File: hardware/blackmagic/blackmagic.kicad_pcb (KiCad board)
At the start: 2 copper layers, 28 parts, among them U1 STM32F411CEUx, U2 USBLC6-2P6, U3 AP2112K-3.3TRG1

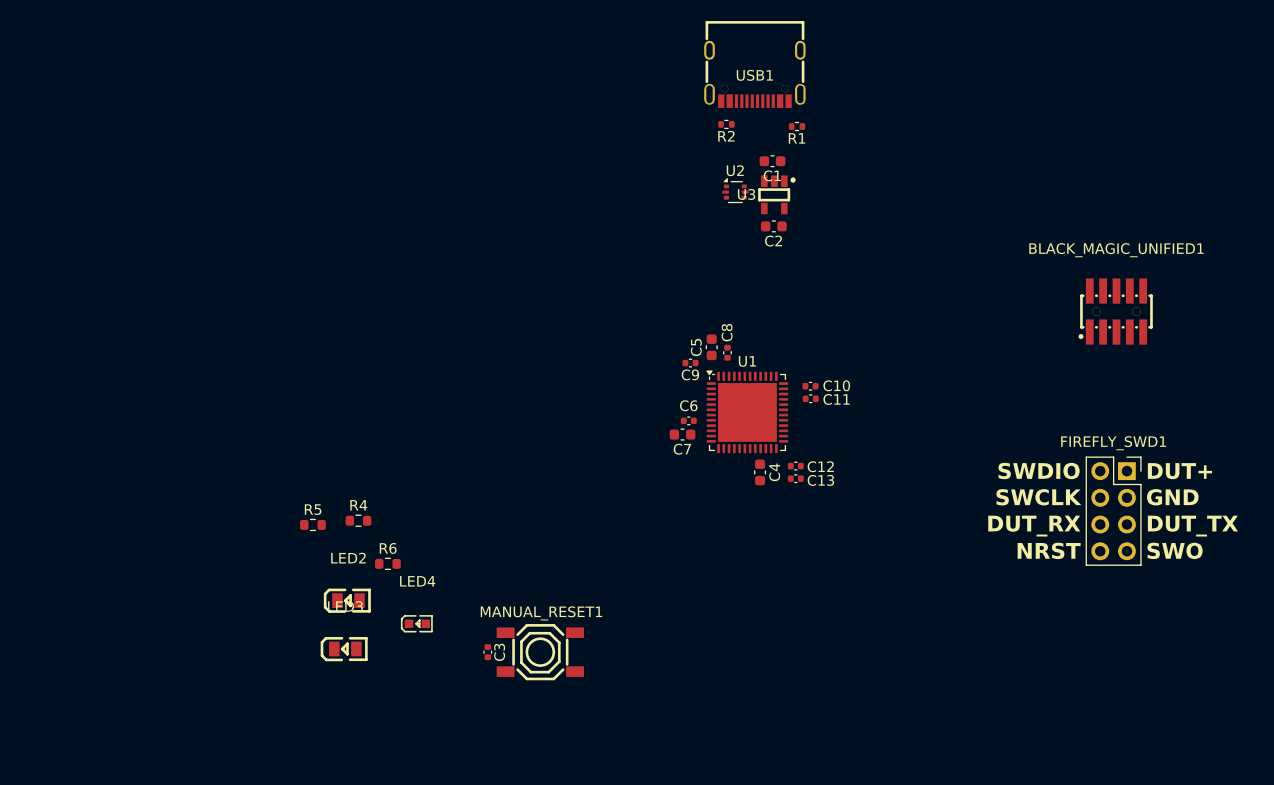
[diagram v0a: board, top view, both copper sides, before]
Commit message: Finish with the first pass of the routing
Still need to add some GND vias and clean things up
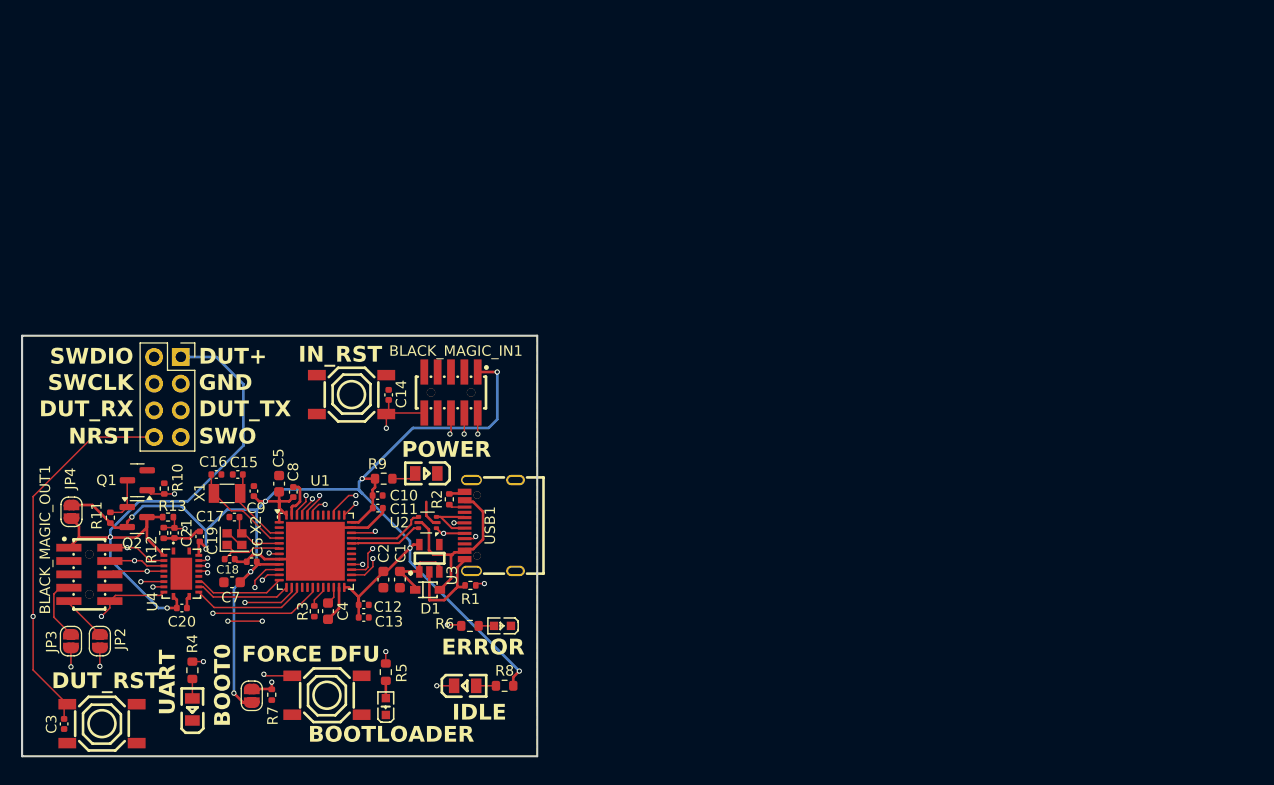
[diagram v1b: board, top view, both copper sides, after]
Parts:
- removed BLACK_MAGIC_UNIFIED1: KH-1.27PH180-2X5P-L7.2-SMT, easyeda2kicad:HDR-SMD_10P-P1.27-V-M-R2-C5-LS5.5
- removed FIREFLY_SWD1: Conn_01x08_Female, Connector_PinSocket_2.54mm:PinSocket_2x04_P2.54mm_Vertical
- removed MANUAL_RESET1: TS-1187A-B-A-B, easyeda2kicad:SW-SMD_4P-L5.1-W5.1-P3.70-LS6.5-TL-2
- added BLACK_MAGIC_IN1: KH-1.27PH180-2X5P-L7.2-SMT, easyeda2kicad:HDR-SMD_10P-P1.27-V-M-R2-C5-LS5.5, F.Cu at (140.8, 105.4)
- added BLACK_MAGIC_OUT1: KH-1.27PH180-2X5P-L7.2-SMT, easyeda2kicad:HDR-SMD_10P-P1.27-V-M-R2-C5-LS5.5, F.Cu at (106.4, 122.7)
- added C14: 100 nF, Capacitor_SMD:C_0402_1005Metric, F.Cu at (134.9, 105.6)
- added C15: 12 pF, Capacitor_SMD:C_0402_1005Metric, F.Cu at (120.5, 113.2)
- added C16: 12 pF, Capacitor_SMD:C_0402_1005Metric, F.Cu at (118.5, 113.2)
- added C17: 12 pF, Capacitor_SMD:C_0402_1005Metric, F.Cu at (120.2, 117.2)
- added C18: 12 pF, Capacitor_SMD:C_0402_1005Metric, F.Cu at (119.8, 121.2)
- added C19: 100 nF, Capacitor_SMD:C_0402_1005Metric, F.Cu at (116.9, 119.1)
- added C20: 100 nF, Capacitor_SMD:C_0402_1005Metric, F.Cu at (115.2, 125.9)
- added C21: 100 nF, Capacitor_SMD:C_0402_1005Metric, F.Cu at (114.5, 118.8)
- added D1: Schottky 1A 40V, easyeda2kicad:SOD-323_L1.8-W1.3-LS2.5-RD, F.Cu at (138.6, 124.2)
- added JP1: SolderJumper_2_Open, Jumper:SolderJumper-2_P1.3mm_Open_RoundedPad1.0x1.5mm, F.Cu at (121.8, 134.2)
- added JP2: SolderJumper_2_Open, Jumper:SolderJumper-2_P1.3mm_Open_RoundedPad1.0x1.5mm, F.Cu at (104.7, 129.1)
- added JP3: SolderJumper_2_Open, Jumper:SolderJumper-2_P1.3mm_Open_RoundedPad1.0x1.5mm, F.Cu at (107.4, 129.1)
- added JP4: SolderJumper_2_Open, Jumper:SolderJumper-2_P1.3mm_Open_RoundedPad1.0x1.5mm, F.Cu at (104.7, 116.8)
- added LED1: Green, easyeda2kicad:LED0805-R-RD, F.Cu at (116.2, 135.6)
- added LED5: Green, easyeda2kicad:LED0805-R-RD, F.Cu at (138.4, 113.1)
- added Q1: 2N7002, Package_TO_SOT_SMD:SOT-23, F.Cu at (111.0, 113.8)
- added Q2: AO3401A, Package_TO_SOT_SMD:SOT-23, F.Cu at (110.9, 117.2)
- added R10: 10k, Resistor_SMD:R_0402_1005Metric, F.Cu at (113.5, 114.5)
- added R11: 10k, Resistor_SMD:R_0402_1005Metric, F.Cu at (108.4, 117.3)
- added R12: 10k, Resistor_SMD:R_0402_1005Metric, F.Cu at (113.5, 118.8)
- added R13: 2K, Resistor_SMD:R_0402_1005Metric, F.Cu at (113.9, 117.2)
- added R3: 10k, Resistor_SMD:R_0402_1005Metric, F.Cu at (127.8, 126.2)
- added R7: 10k, Resistor_SMD:R_0402_1005Metric, F.Cu at (123.8, 134.2)
- added R8: 330R, Resistor_SMD:R_0603_1608Metric, F.Cu at (145.9, 133.3)
- added R9: 330R, Resistor_SMD:R_0603_1608Metric, F.Cu at (134.4, 113.6)
- added SW1: TS-1187A-B-A-B, easyeda2kicad:SW-SMD_4P-L5.1-W5.1-P3.70-LS6.5-TL-2, F.Cu at (107.6, 136.9)
- added SW2: TS-1187A-B-A-B, easyeda2kicad:SW-SMD_4P-L5.1-W5.1-P3.70-LS6.5-TL-2, F.Cu at (131.3, 105.6)
- added SW3: TS-1187A-B-A-B, easyeda2kicad:SW-SMD_4P-L5.1-W5.1-P3.70-LS6.5-TL-2, F.Cu at (129.0, 134.2)
- added SWD_OUT1: Conn_01x08_Female, Connector_PinSocket_2.54mm:PinSocket_2x04_P2.54mm_Vertical, F.Cu at (115.1, 102.0)
- added U4: TXS0108ERGYR, easyeda2kicad:VQFN-20_L4.6-W3.6-P0.50-BL-EP, F.Cu at (115.2, 122.6)
- added X1: 32.768kHz crystal, Crystal:Crystal_SMD_3215-2Pin_3.2x1.5mm, F.Cu at (119.5, 115.0)
- added X2: 25Mhz crystal, Crystal:Crystal_SMD_2016-4Pin_2.0x1.6mm, F.Cu at (120.2, 119.3)
- LED2: value 0805G (Green) -> Yellow
- LED3: value 17-21SUYC/TR8 -> White; footprint easyeda2kicad:LED0805-R-RD -> easyeda2kicad:LED0603-R-RD_WHITE
- LED4: value KT-0603R -> Red
- moved R1 53.6 mm to (142.7, 123.8), turned to 0 degrees
- moved C1 53.3 mm to (135.9, 123.2), turned to -90 degrees
- moved C2 50.1 mm to (134.4, 123.2), turned to -90 degrees
- moved USB1 49.6 mm to (144.5, 118.0), turned to 90 degrees
- moved U3 47.7 mm to (138.7, 121.2), turned to 0 degrees
- moved C7 45.1 mm to (120.0, 123.5)
- moved R2 44.3 mm to (140.6, 115.6), turned to 90 degrees
- moved C6 43.7 mm to (121.8, 121.5)
- moved C8 43.4 mm to (125.8, 114.9)
- moved C9 43.3 mm to (122.0, 114.8), turned to 90 degrees
- moved C13 43.2 mm to (132.5, 126.8)
- moved C4 43.2 mm to (129.1, 126.2)
- moved U1 43.2 mm to (127.9, 120.5)
- moved C12 43.2 mm to (132.5, 125.6)
- moved C5 43.1 mm to (124.5, 114.1)
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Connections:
- C1 pad 1: VBUS -> Net-(D1-C)
- LED2 pad 1: Net-(LED2-A) -> Net-(LED2-+)
- LED2 pad 2: GND -> /LED_IDLE
- R4 pad 1: Net-(LED2-A) -> Net-(LED1-A)
- U1 pad 10: unconnected-(U1-PA0-Pad10) -> /FORCE_DFU
- U1 pad 11: unconnected-(U1-PA1-Pad11) -> /PWR_BR
- U1 pad 18: unconnected-(U1-PB0-Pad18) -> /TPWR
- U1 pad 20: unconnected-(U1-PB2-Pad20) -> /BOOT1
- U1 pad 26: unconnected-(U1-PB13-Pad26) -> /LED_IDLE
- U1 pad 27: unconnected-(U1-PB14-Pad27) -> /LED_ERROR
- U1 pad 28: unconnected-(U1-PB15-Pad28) -> /LED_BOOTLOADER
- U1 pad 3: unconnected-(U1-PC14-Pad3) -> /OSC32_IN
- U1 pad 34: unconnected-(U1-PA13-Pad34) -> /IN_SWDIO
- U1 pad 37: unconnected-(U1-PA14-Pad37) -> /IN_SWCLK
- U1 pad 39: unconnected-(U1-PB3-Pad39) -> /IN_SWO
- U1 pad 4: unconnected-(U1-PC15-Pad4) -> /OSC32_OUT
- U1 pad 44: unconnected-(U1-BOOT0-Pad44) -> /BOOT0
- U1 pad 5: unconnected-(U1-PH0-Pad5) -> /OSC_IN
- U1 pad 6: unconnected-(U1-PH1-Pad6) -> /OSC_OUT
- U1 pad 7: unconnected-(U1-NRST-Pad7) -> /IN_NRST
- U3 pad 1: VBUS -> Net-(D1-C)
- U3 pad 3: VBUS -> Net-(D1-C)
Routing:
- net +3V3: track 0.00 -> 137.4 mm, vias 0 -> 9
- net DUT+: track 0.00 -> 58.3 mm, vias 0 -> 2
- net /DUT_NRST: track 0.00 -> 50.3 mm, vias 0 -> 2
- net GND: track 0.00 -> 44.9 mm
- net /DUT_RX: track 0.00 -> 33.8 mm, vias 0 -> 2
- net /DUT_TX: track 0.00 -> 32.1 mm, vias 0 -> 2
- net /PWR_BR: track 0.00 -> 25.9 mm, vias 0 -> 4
- net /BOOT0: track 0.00 -> 25.8 mm, vias 0 -> 2
- net /IN_NRST: track 0.00 -> 25.8 mm, vias 0 -> 2
- net /DUT_SWDIO: track 0.00 -> 24.9 mm, vias 0 -> 1
- net /TPWR: track 0.00 -> 23.1 mm, vias 0 -> 2
- net /DUT_SWCLK: track 0.00 -> 23.0 mm, vias 0 -> 1
- net /DUT_SWO: track 0.00 -> 20.5 mm, vias 0 -> 1
- net /IN_SWDIO: track 0.00 -> 20.2 mm, vias 0 -> 2
- net /LED_IDLE: track 0.00 -> 19.4 mm, vias 0 -> 2
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- added copper zone on F.Cu, net GND
- added copper zone on In1.Cu, net GND
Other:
- board outline added: 49 x 40 mm
- copper layers 2 -> 4
- board text added: "BOOT0"
- board text added: "BOOTLOADER"
- board text added: "DUT_RST"
- board text added: "ERROR"
- board text added: "FORCE DFU"
- board text added: "IDLE"
- board text added: "IN_RST"
- board text added: "POWER"
- board text added: "UART"

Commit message: Run cleanup pass
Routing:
- net GND: track 44.9 -> 39.7 mm
- net Net-(JP2-A): track 6.18 -> 5.35 mm
- net +3V3: track 137.4 -> 136.8 mm
- net /OSC_IN: track 5.60 -> 5.09 mm

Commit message: Finish blackmagic board and send it to production
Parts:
- added H1: MountingHole, MountingHole:MountingHole_2.2mm_M2, F.Cu at (102.3, 102.5)
- added H2: MountingHole, MountingHole:MountingHole_2.2mm_M2, F.Cu at (146.6, 102.4)
- added H3: MountingHole, MountingHole:MountingHole_2.2mm_M2, F.Cu at (146.5, 137.5)
- added H4: MountingHole, MountingHole:MountingHole_2.2mm_M2, F.Cu at (102.5, 137.5)
- U1: footprint Package_DFN_QFN:QFN-48-1EP_7x7mm_P0.5mm_EP5.6x5.6mm -> easyeda2kicad:UFQFPN-48_L7.0-W7.0-P0.50-BL-EP
- U2: footprint Package_TO_SOT_SMD:SOT-666 -> easyeda2kicad:SOT-666-6_L1.6-W1.2-P0.50-LS1.6-BR
- moved C3 2.40 mm to (106.4, 136.9)
- moved SW1 2.40 mm to (110.0, 136.9)
- turned U1 to -90 degrees
- turned U2 to 0 degrees
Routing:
- net GND: track 39.7 -> 60.2 mm, vias 0 -> 25
- net VBUS: track 17.7 -> 20.8 mm, vias 0 -> 2
- net /DUT_NRST: track 49.8 -> 52.7 mm
- net +3V3: track 136.8 -> 135.7 mm
- net /D+: track 7.34 -> 8.02 mm
